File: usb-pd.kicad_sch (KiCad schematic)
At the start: 71 parts, among them J3 USB-C_GCT_USB4105-GF-A, J4 JST_SH_1x4_SM04B-SRSS-TB-LF-SN, Q4 SQS401EN-T1_BE3, U2 TVS2200DRVR, U5 TPD4E02B04DQA, U6 STUSB4500_QFN, U9 SIC477ED-T1-GE3

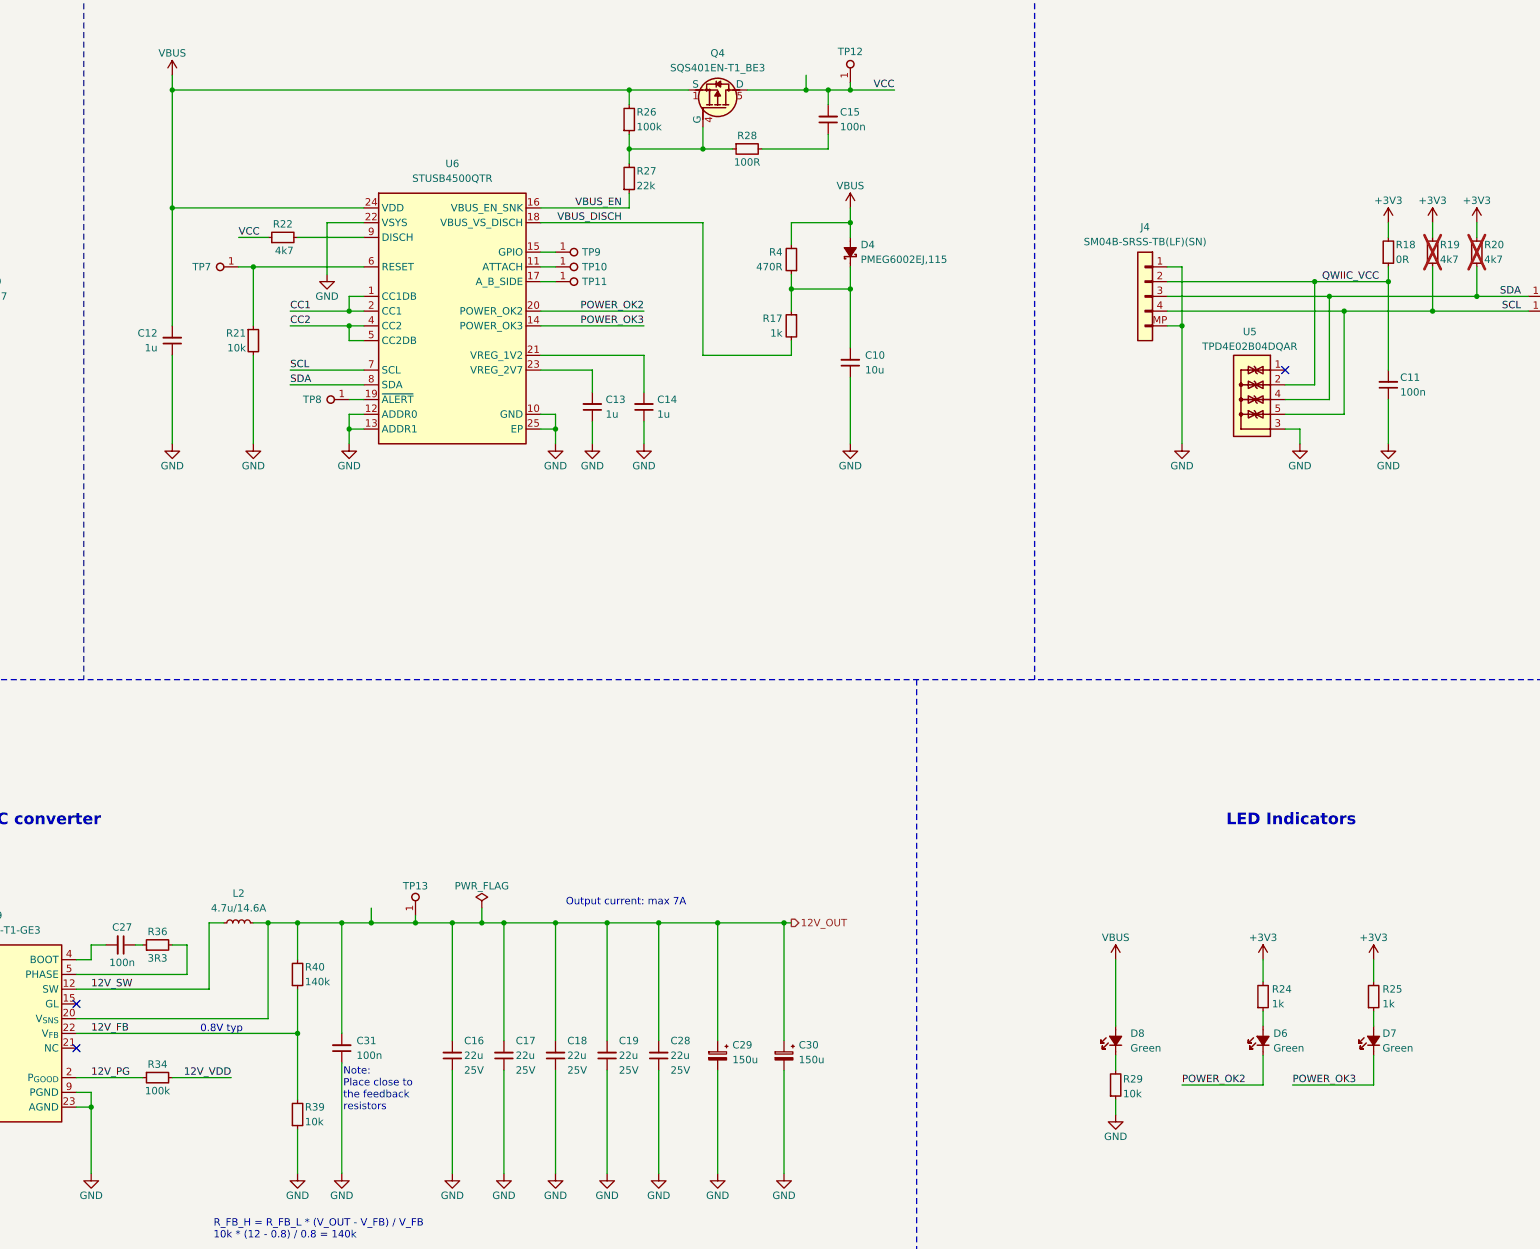
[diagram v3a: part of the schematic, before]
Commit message: [#79262] BOM consolidation
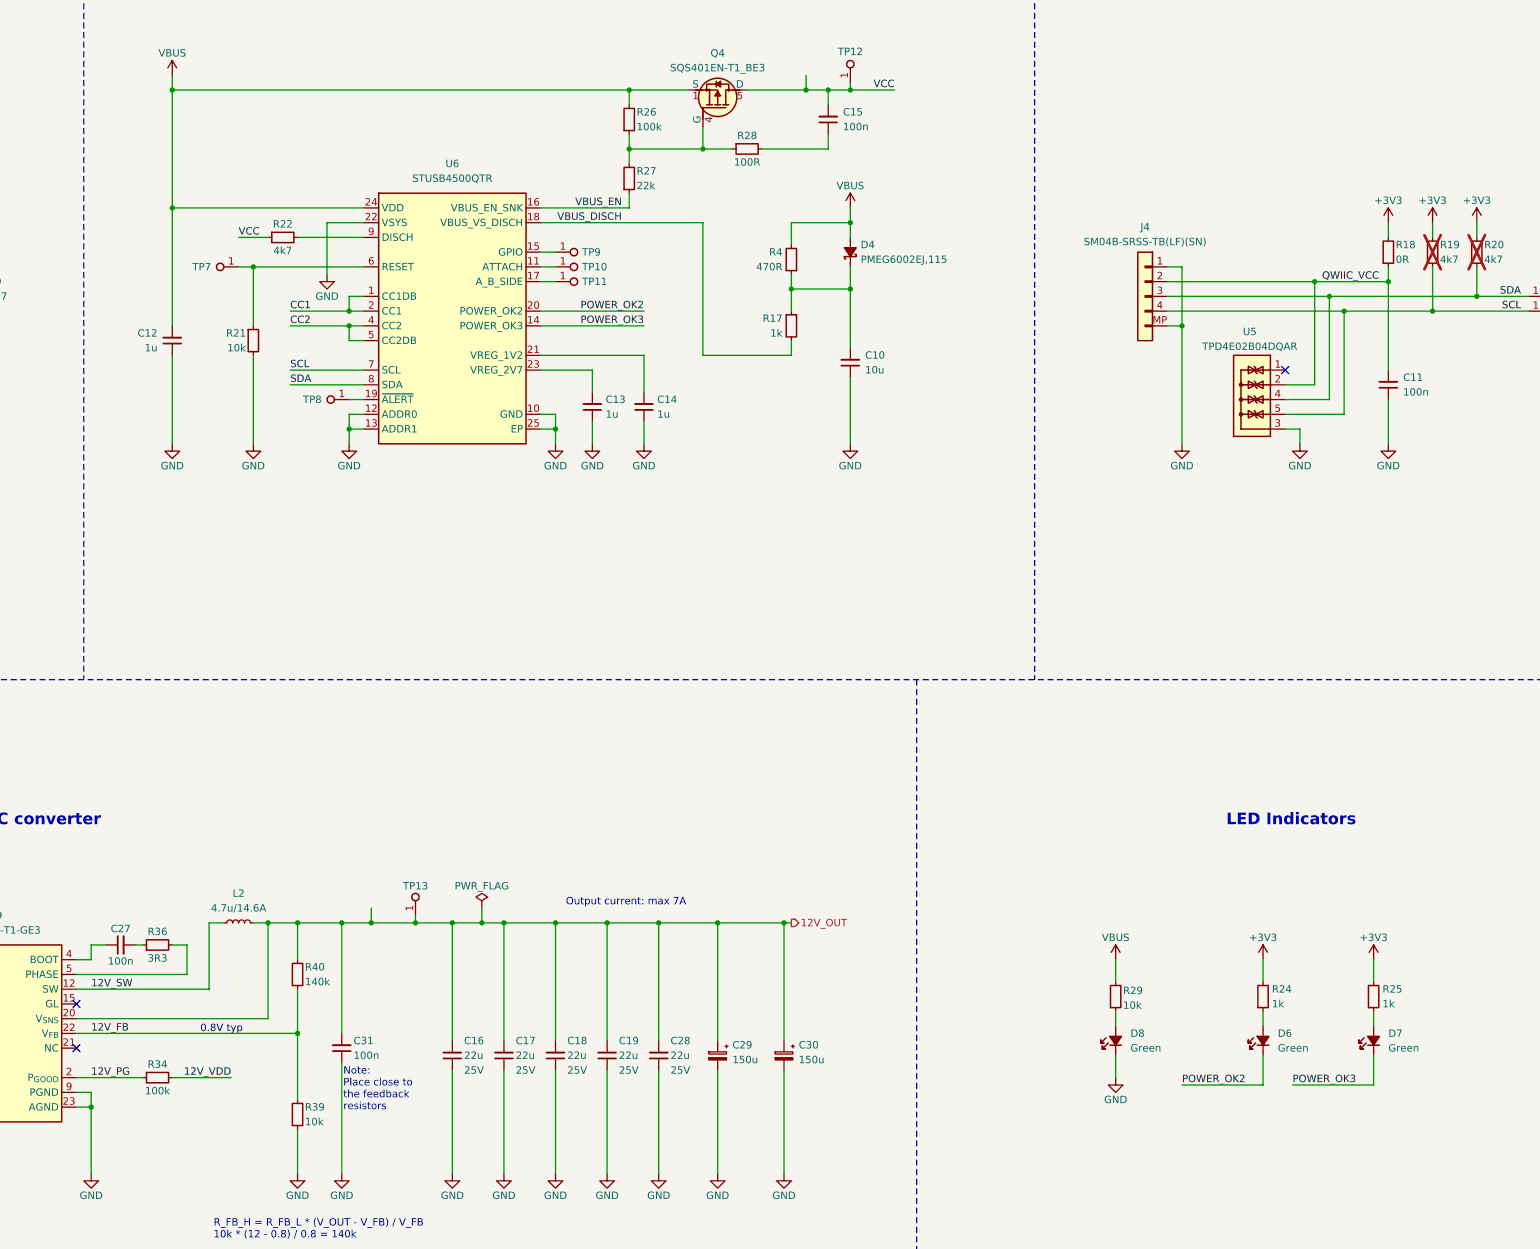
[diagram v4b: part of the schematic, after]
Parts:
- removed C11, C15, C26, C27, C31: C_100n_50V_X8L_0402, antmicro-footprints:C_0402_1005Metric, symbol antmicroCapacitors0402:C_100n_50V_X8L_0402
- removed D6, D7: LED_G_0603_LG_L29K-G2J1-24-Z, antmicro-footprints:LED_0603_1608Metric_G, symbol antmicroLEDIndicationDiscrete:LED_G_0603_LG_L29K-G2J1-24-Z
- removed R22: R_4k7_0603, antmicro-footprints:R_0603_1608Metric, symbol antmicroResistors0603:R_4k7_0603
- added C11, C15, C26, C27, C31: C_100n_0402, antmicro-footprints:C_0402_1005Metric, symbol antmicroCapacitors0402:C_100n_0402
- added D6, D7: LED_G_0603_LTST-C190GKT, antmicro-footprints:LED_0603_1608Metric_G, symbol antmicroLEDIndicationDiscrete:LED_G_0603_LTST-C190GKT
- added R22: R_4k7_0402, antmicro-footprints:R_0402_1005Metric, symbol antmicroResistors0402:R_4k7_0402
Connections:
- net 12V_OUT: now also C31.2
- net GND: now also D8.1 (C), C11.1, C26.1, C31.1; no longer R29.1
- net POWER_OK2: now also D6.1 (C)
- net POWER_OK3: now also D7.1 (C)
- net QWIIC_VCC: now also C11.2
- net VBUS: now also R29.2; no longer D8.2 (A)
- net VCC: now also C15.2, C26.2, R22.1
- net at U6.9 (DISCH): now also R22.2
- net at R36.1: now also C27.2
- net at R24.1: now also D6.2 (A)
- net at R28.2: now also C15.1
- net at R25.1: now also D7.2 (A)
- net at U9.4 (BOOT): now also C27.1
- new net: D8.2 (A), R29.1
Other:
- moved on the sheet: R29

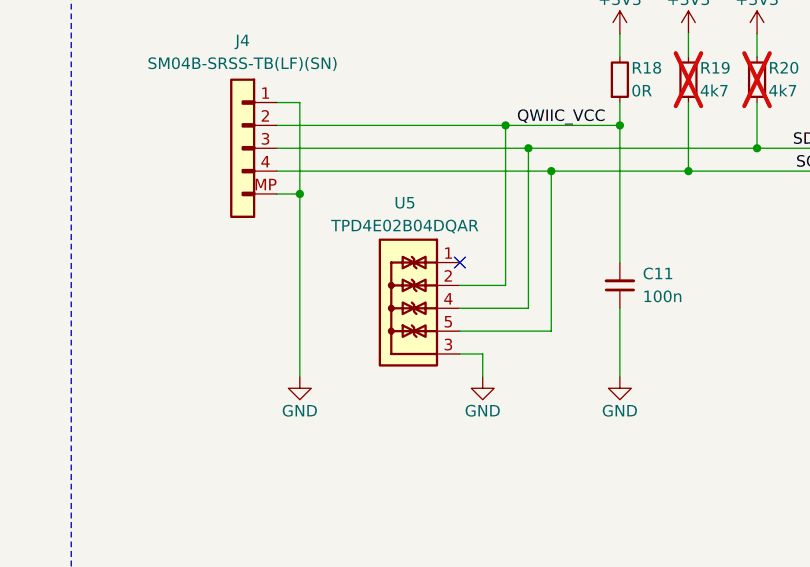
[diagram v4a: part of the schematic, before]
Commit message: [#79262] Further BOM consolidation
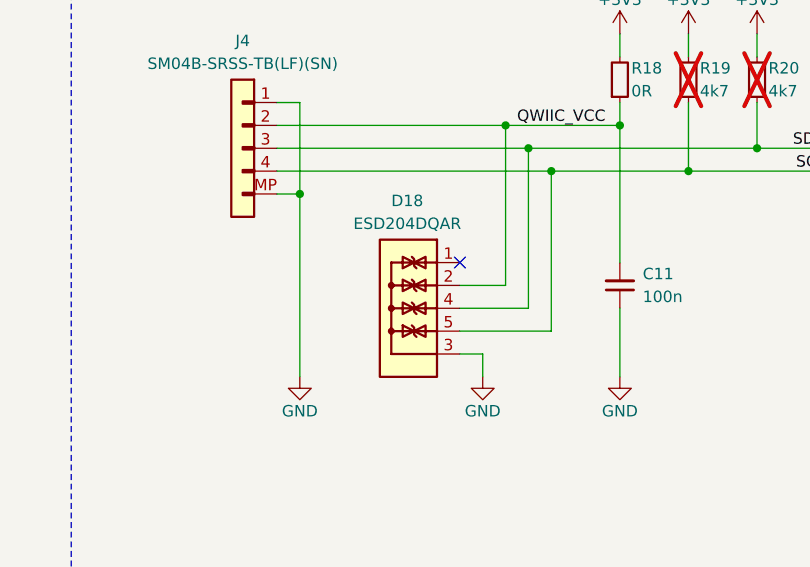
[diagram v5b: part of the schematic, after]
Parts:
- removed U5: TPD4E02B04DQA, antmicro-footprints:USON-10_2.5x1mm_P0.5mm, symbol antmicroTVSDiodes:TPD4E02B04DQA
- added D18: ESD204DQAR, antmicro-footprints:USON-10_2.5x1mm_P0.5mm, symbol antmicroTVSDiodes:ESD204DQAR
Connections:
- net GND: now also D18.3, D18.8
- net QWIIC_VCC: now also D18.2, D18.9
- net SCL: now also D18.5, D18.6
- net SDA: now also D18.4, D18.7
- new net: D18.1, D18.10
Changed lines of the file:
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@@
+	)
+	(symbol
+		(lib_id "antmicroTVSDiodes:ESD204DQAR")
+		(at 353.06 99.06 0)
+		(mirror y)
+		(unit 1)
+		(exclude_from_sim no)
+		(in_bom yes)
+		(on_board yes)
+		(dnp no)
+		(property "Reference" "D18"
+			(at 347.218 92.202 0)
+			(effects
+				(font
+					(size 1.27 1.27)
+					(thickness 0.15)
+				)
+			)
+		)
+		(property "Value" "ESD204DQAR"
+			(at 328.93 104.14 0)
+			(effects
+				(font
+					(size 1.27 1.27)
+					(thickness 0.15)
+				)
+				(justify left bottom)
+				(hide yes)
+			)
+		)
+		(property "Footprint" "antmicro-footprints:USON-10_2.5x1mm_P0.5mm"
+			(at 328.93 106.68 0)
+			(effects
+				(font
+					(size 1.27 1.27)
+					(thickness 0.15)
+				)
+				(justify left bottom)
+				(hide yes)
+			)
+		)
+		(property "Datasheet" "https://www.ti.com/lit/ds/symlink/esd204.pdf?ts=1706004844383&ref_url=https%253A%252F%252Fwww.ti.com%252Finterface%252Fdiodes%252Fesd-protection-diodes%252Fproducts.html"
+			(at 328.93 109.22 0)
+			(effects
+				(font
+					(size 1.27 1.27)
+					(thickness 0.15)
+				)
+				(justify left bottom)
+				(hide yes)
+			)
+		)
+		(property "Description" "TVS diode array, 30 kV, USON-10, 3.6 V, 0.55 pF"
+			(at 328.93 119.38 0)
+			(effects
+				(font
+					(size 1.27 1.27)
+				)
+				(justify left bottom)
+				(hide yes)
+			)
+		)
+		(property "MPN" "ESD204DQAR"
+			(at 347.218 94.742 0)
+			(effects
+				(font
+					(size 1.27 1.27)
+					(thickness 0.15)
+				)
+			)
+		)
+		(property "Manufacturer" "Texas Instruments"
+			(at 328.93 111.76 0)
+			(effects
+				(font
+					(size 1.27 1.27)
+					(thickness 0.15)
+				)
+				(justify left bottom)
+				(hide yes)
+			)
+		)
+		(property "Author" "Antmicro"
+			(at 328.93 114.3 0)
+			(effects
+				(font
+					(size 1.27 1.27)
+					(thickness 0.15)
+				)
+				(justify left bottom)
+				(hide yes)
+			)
+		)
+		(property "License" "Apache-2.0"
+			(at 328.93 116.84 0)
+			(effects
+				(font
+					(size 1.27 1.27)
+					(thickness 0.15)
+				)
+				(justify left bottom)
+				(hide yes)
+			)
+		)
+		(pin "7"
+		)
+		(pin "5"
+		)
+		(pin "8"
+		)
+		(pin "1"
+		)
+		(pin "6"
+		)
+		(pin "3"
+		)
+		(pin "10"
+		)
+		(pin "2"
+		)
+		(pin "4"
+		)
+		(pin "9"
+		)
+		(instances
+			(project "oculink-to-pcie-adapter"
+				(path "/44c3be85-0a18-4d93-a9a5-650ee09b6032/967dc2ce-6faa-4f65-adf2-eb5d333aef74"
+					(reference "D18")
+					(unit 1)
+				)
+			)
+		)
 	)
 	(symbol
@@
 					(unit 1)
 				)
-			)
-		)
-	)
-	(symbol
-		(lib_id "antmicroTVSDiodes:TPD4E02B04DQA")
-		(at 353.06 99.06 0)
-		(mirror y)
-		(unit 1)
-		(exclude_from_sim no)
-		(in_bom yes)
-		(on_board yes)
-		(dnp no)
-		(property "Reference" "U5"
-			(at 346.964 92.456 0)
-			(effects
-				(font
-					(size 1.27 1.27)
-					(thickness 0.15)
-				)
-			)
-		)
-		(property "Value" "TPD4E02B04DQA"
-			(at 342.9 111.76 90)
-			(effects
-				(font
-					(size 1.27 1.27)
-					(thickness 0.15)
-				)
-				(justify left)
-				(hide yes)
-			)
-		)
-		(property "Footprint" "antmicro-footprints:USON-10_2.5x1mm_P0.5mm"
-			(at 340.36 104.14 0)
-			(effects
-				(font
-					(size 1.27 1.27)
-					(thickness 0.15)
-				)
-				(justify left bottom)
-				(hide yes)
-			)
-		)
-		(property "Datasheet" "http://www.ti.com/lit/ds/symlink/tpd4e02b04.pdf"
-			(at 340.36 106.68 0)
-			(effects
-				(font
-					(size 1.27 1.27)
-					(thickness 0.15)
-				)
-				(justify left bottom)
-				(hide yes)
-			)
-		)
-		(property "Description" "TVS diode array, 12 kV, USON-10, 3.6 V, 0.33 pF"
-			(at 353.06 99.06 0)
-			(effects
-				(font
-					(size 1.27 1.27)
-				)
-				(hide yes)
-			)
-		)
-		(property "MPN" "TPD4E02B04DQAR"
-			(at 346.964 94.996 0)
-			(effects
-				(font
-					(size 1.27 1.27)
-					(thickness 0.15)
-				)
-			)
-		)
-		(property "Manufacturer" "Texas Instruments"
-			(at 340.36 111.76 0)
-			(effects
-				(font
-					(size 1.27 1.27)
-					(thickness 0.15)
-				)
-				(justify left bottom)
-				(hide yes)
-			)
-		)
-		(property "Author" "Antmicro"
-			(at 340.36 114.3 0)
-			(effects
-				(font
-					(size 1.27 1.27)
-					(thickness 0.15)
-				)
-				(justify left bottom)
-				(hide yes)
-			)
-		)
-		(property "License" "Apache-2.0"
-			(at 340.36 116.84 0)
-			(effects
-				(font
-					(size 1.27 1.27)
-					(thickness 0.15)
-				)
-				(justify left bottom)
-				(hide yes)
-			)
-		)
-		(pin "1"
-		)
-		(pin "9"
-		)
-		(pin "2"
-		)
-		(pin "7"
-		)
-		(pin "5"
-		)
-		(pin "6"
-		)
-		(pin "3"
-		)
-		(pin "8"
-		)
-		(pin "10"
-		)
-		(pin "4"
-		)
-		(instances
-			(project "oculink-to-pcie-adapter"
-				(path "/44c3be85-0a18-4d93-a9a5-650ee09b6032/967dc2ce-6faa-4f65-adf2-eb5d333aef74"
-					(reference "U5")
-					(unit 1)
-				)
